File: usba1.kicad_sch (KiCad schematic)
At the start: 28 parts, among them U10 RH792A, U11 XXL1509-5.0, U12 XXL1509-5.0, U13 XDUF-0426-081_C18202150, U14 XXL1509-5.0, U15 XXL1509-5.0, U8 RH792A, U9 XDUF-0426-081_C18202150

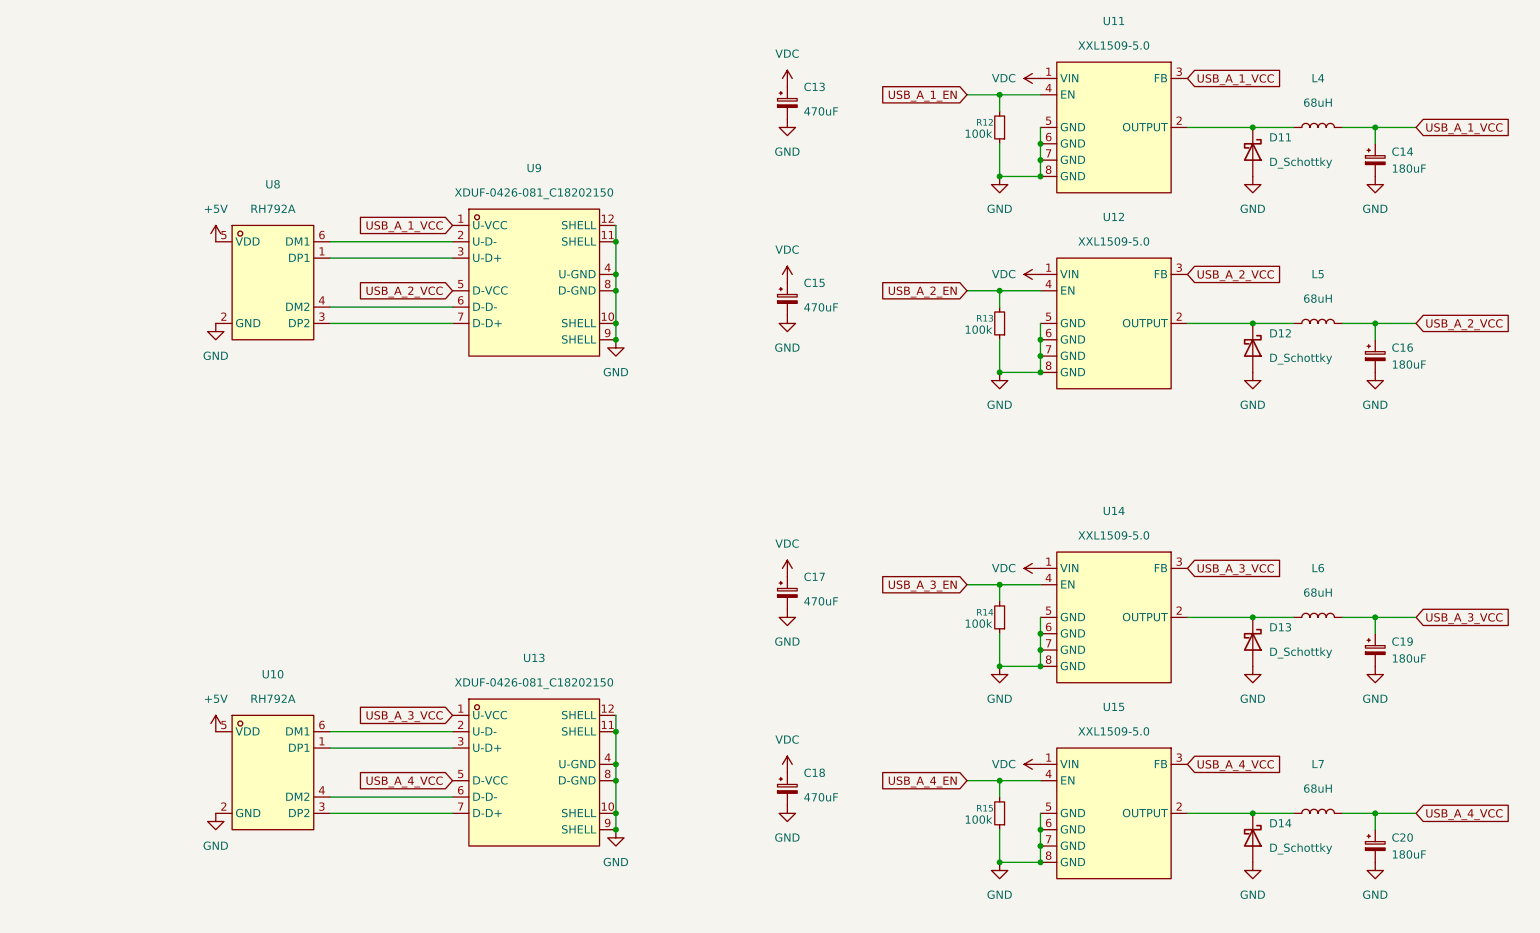
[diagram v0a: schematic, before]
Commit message: gave up on single board, gonna make small modules
Signed-off-by: Toby Cm <toby@vsus.app>
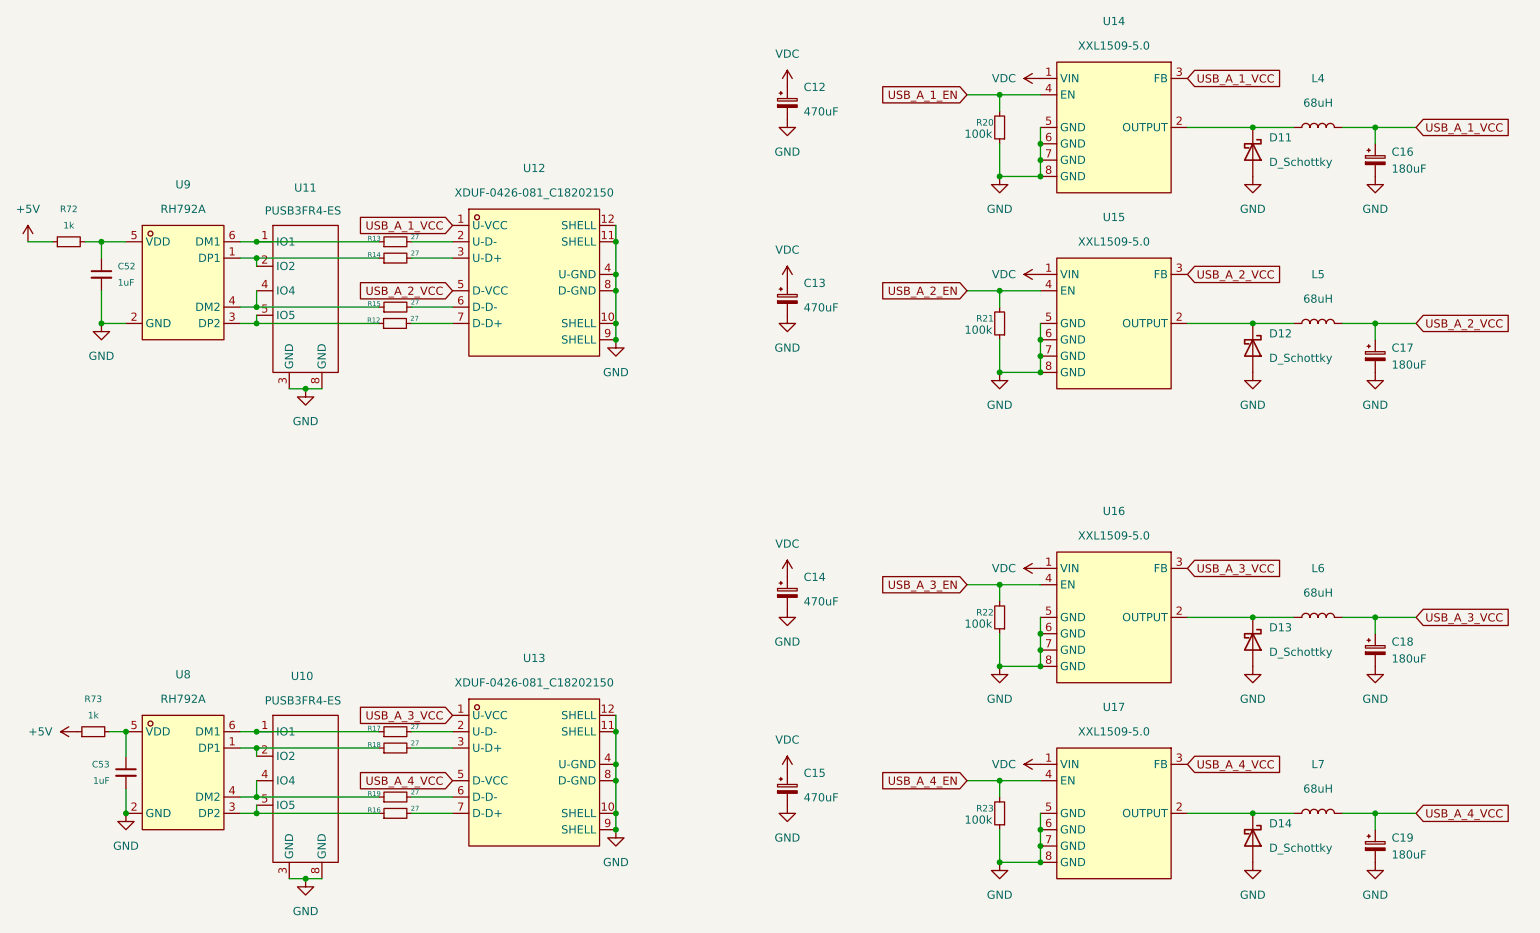
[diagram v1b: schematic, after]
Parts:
- added C52, C53: 1uF, Capacitor_SMD:C_0402_1005Metric_Pad0.74x0.62mm_HandSolder, symbol Device:C_Small
- added R12, R13, R14, R15, R16, R17, R18, R19: 27, Resistor_SMD:R_0402_1005Metric_Pad0.72x0.64mm_HandSolder, symbol Device:R_Small
- added R72, R73: 1k, Resistor_SMD:R_0402_1005Metric_Pad0.72x0.64mm_HandSolder, symbol Device:R_Small
- added U10, U11: PUSB3FR4-ES, Package_DFN_QFN:Diodes_UDFN-10_1.0x2.5mm_P0.5mm, symbol ElecSuper:PUSB3FR4-ES
- C12: renamed from C13; footprint (none) -> Capacitor_THT:CP_Radial_D17.0mm_P7.50mm
- C13: renamed from C15; footprint (none) -> Capacitor_THT:CP_Radial_D17.0mm_P7.50mm
- C14: renamed from C17; footprint (none) -> Capacitor_THT:CP_Radial_D17.0mm_P7.50mm
- C15: renamed from C18; footprint (none) -> Capacitor_THT:CP_Radial_D17.0mm_P7.50mm
- C16: renamed from C14; footprint (none) -> Capacitor_THT:CP_Radial_D8.0mm_P5.00mm
- C17: renamed from C16; footprint (none) -> Capacitor_THT:CP_Radial_D8.0mm_P5.00mm
- C18: renamed from C19; footprint (none) -> Capacitor_THT:CP_Radial_D8.0mm_P5.00mm
- C19: renamed from C20; footprint (none) -> Capacitor_THT:CP_Radial_D8.0mm_P5.00mm
- D11, D12, D13, D14: footprint (none) -> Diode_SMD:D_SMB_Handsoldering
- L4, L5, L6, L7: footprint (none) -> easyeda2kicad:IND-SMD_L8.0-W8.0-1
- R20: renamed from R12; footprint (none) -> Resistor_SMD:R_0402_1005Metric_Pad0.72x0.64mm_HandSolder
- R21: renamed from R13; footprint (none) -> Resistor_SMD:R_0402_1005Metric_Pad0.72x0.64mm_HandSolder
- R22: renamed from R14; footprint (none) -> Resistor_SMD:R_0402_1005Metric_Pad0.72x0.64mm_HandSolder
- R23: renamed from R15; footprint (none) -> Resistor_SMD:R_0402_1005Metric_Pad0.72x0.64mm_HandSolder
- renumbered U9 to U12, U11 to U14, U12 to U15, U14 to U16, U15 to U17, U10 to U8, U8 to U9
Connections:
- net +5V: now also R72.1, R73.1; no longer U8.5 (VDD), U9.5 (VDD)
- net GND: now also C52.2, C53.2, U10.3 (GND), U10.8 (GND), U11.3 (GND), U11.8 (GND)
- net at U9.1 (DP1): now also R14.1, U11.2 (IO2); no longer U12.3 (U-D+)
- net at U9.3 (DP2): now also R12.1, U11.5 (IO5); no longer U12.7 (D-D+)
- net at U9.4 (DM2): now also R15.1, U11.4 (IO4); no longer U12.6 (D-D-)
- net at U9.6 (DM1): now also R13.1, U11.1 (IO1); no longer U12.2 (U-D-)
- net at U8.1 (DP1): now also R18.1, U10.2 (IO2); no longer U13.3 (U-D+)
- net at U8.3 (DP2): now also R16.1, U10.5 (IO5); no longer U13.7 (D-D+)
- net at U8.4 (DM2): now also R19.1, U10.4 (IO4); no longer U13.6 (D-D-)
- net at U8.6 (DM1): now also R17.1, U10.1 (IO1); no longer U13.2 (U-D-)
- new net: C53.1, R73.2, U8.5 (VDD)
- new net: R19.2, U13.6 (D-D-)
- new net: C52.1, R72.2, U9.5 (VDD)
- new net: R13.2, U12.2 (U-D-)
- new net: R16.2, U13.7 (D-D+)
- new net: R17.2, U13.2 (U-D-)
- new net: R15.2, U12.6 (D-D-)
- new net: R14.2, U12.3 (U-D+)
- new net: R12.2, U12.7 (D-D+)
- new net: R18.2, U13.3 (U-D+)
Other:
- moved on the sheet: U8, U9
